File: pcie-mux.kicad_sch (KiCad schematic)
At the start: 25 parts, among them Q4 BSS138PW,115, Q5 BSS138PW,115, SW1 SW_CVS-02B, U11 SY75602BTWL-TR, U4 TMUXHS4412RUAR, U8 74LVC1G157-Q100H_SOT457

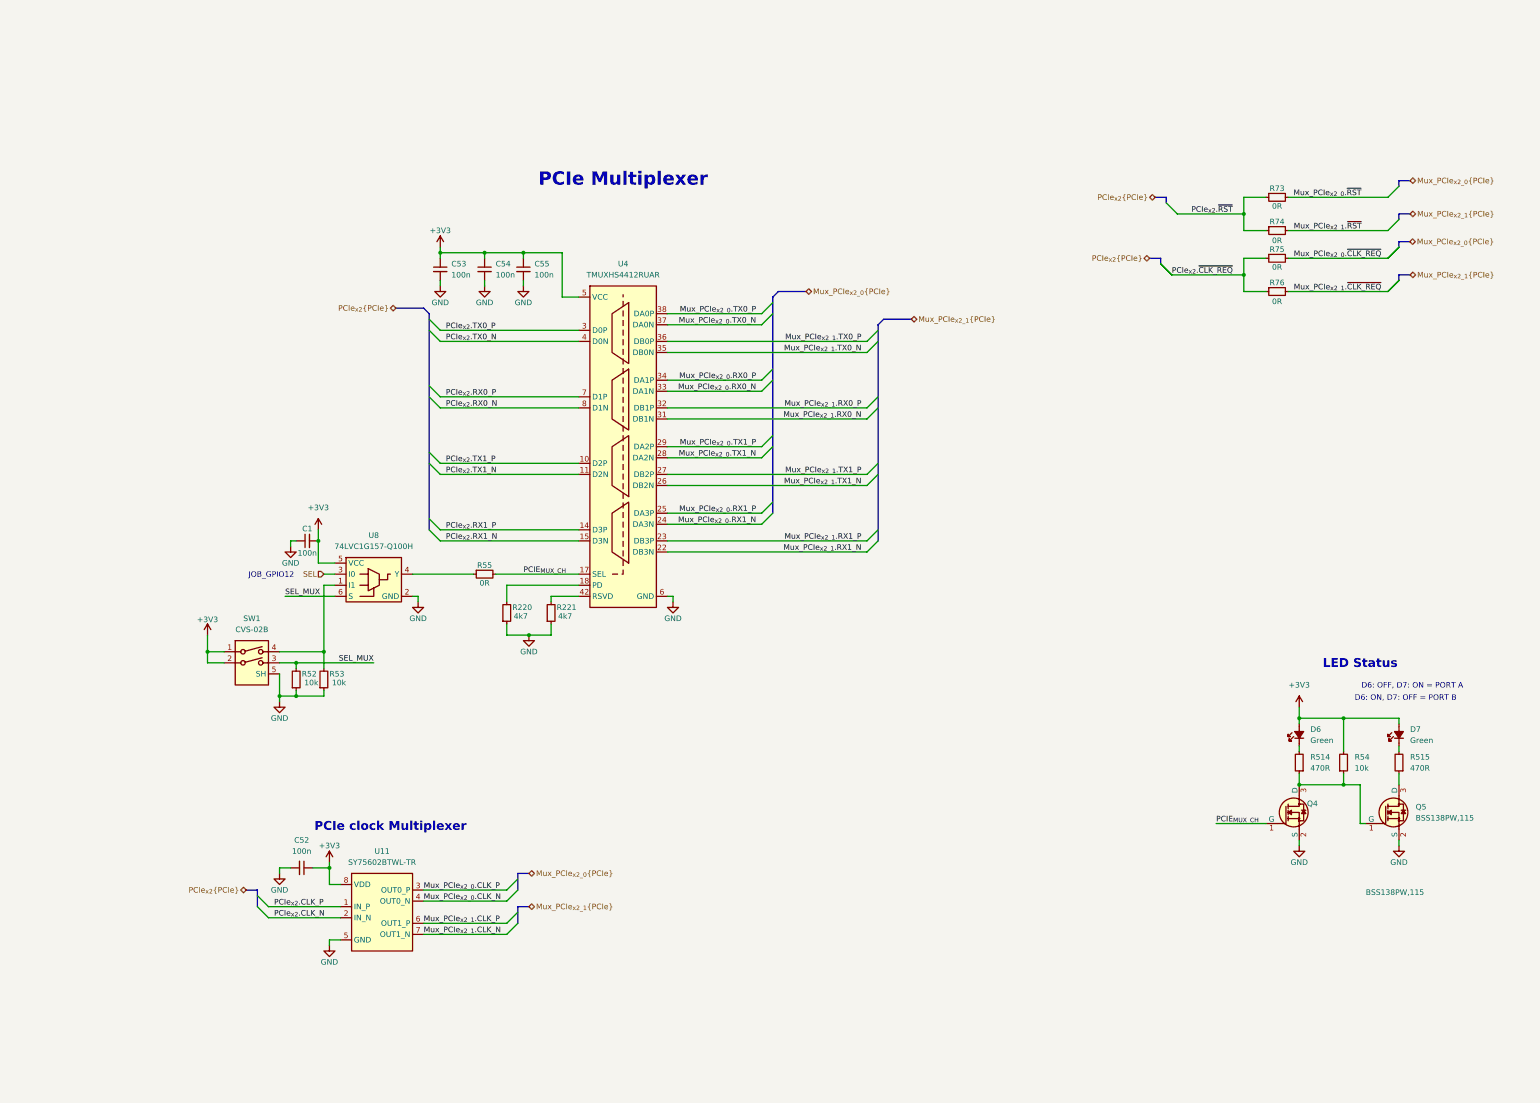
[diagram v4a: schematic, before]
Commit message: [#100765] WIP: Apply review changes
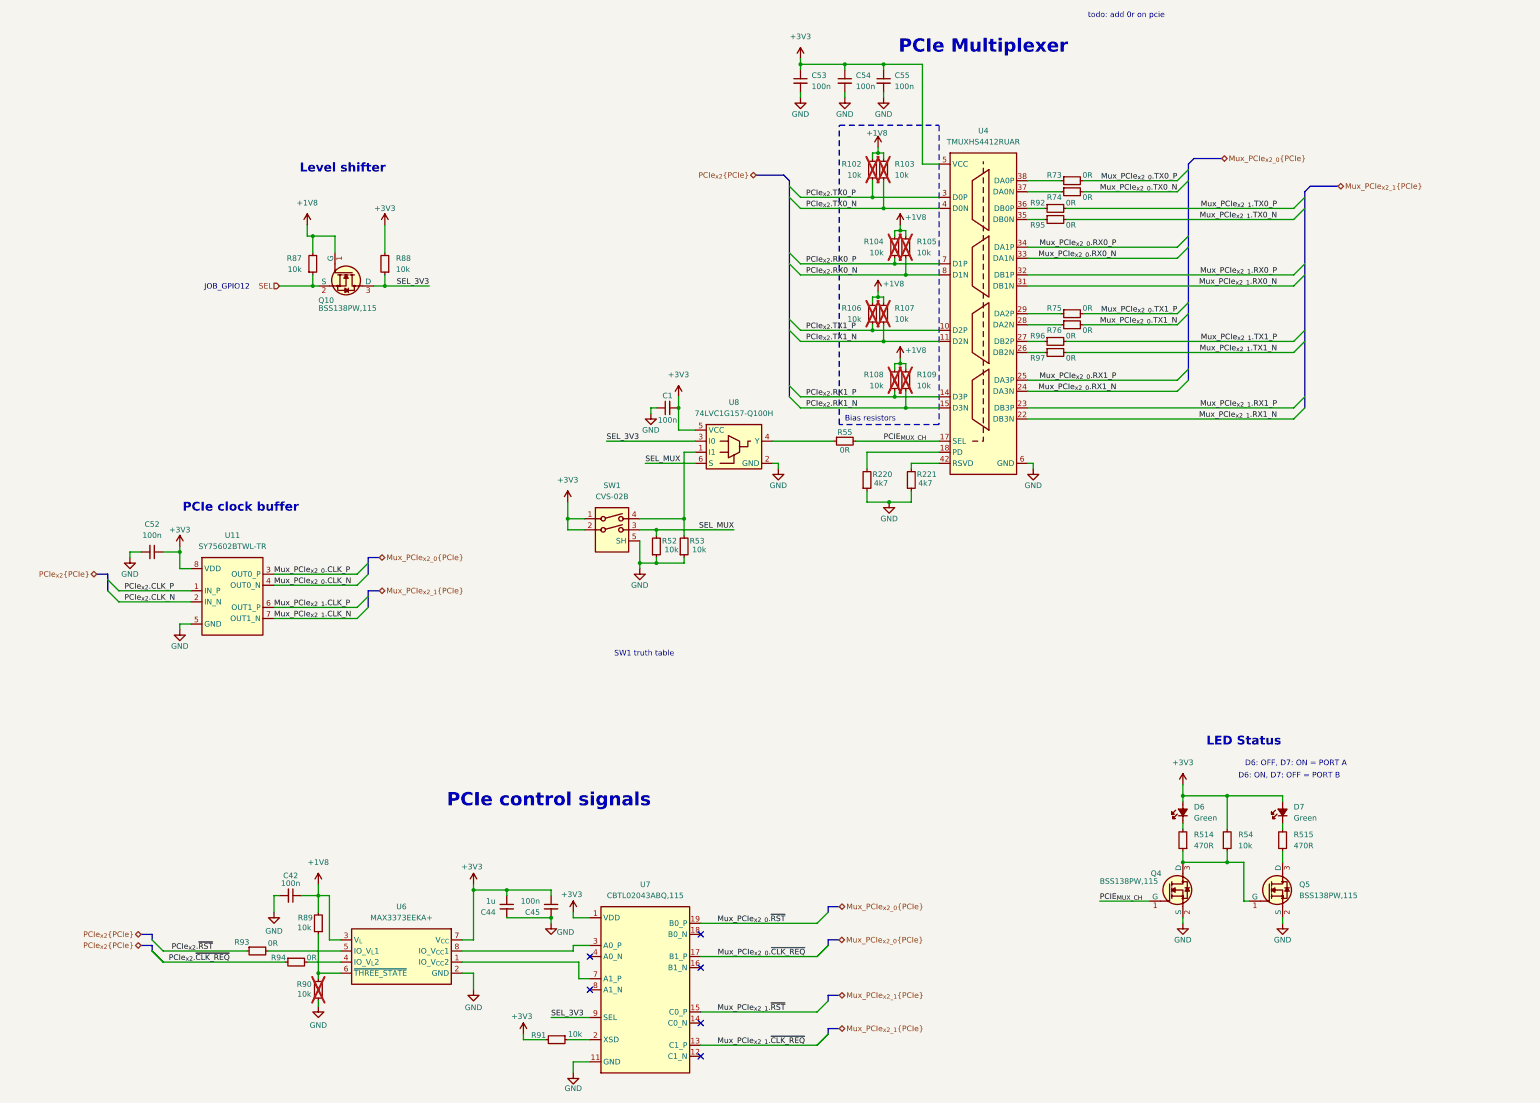
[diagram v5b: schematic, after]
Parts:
- added C42, C45: C_100n_0402, antmicro-footprints:C_0402_1005Metric, symbol antmicroCapacitors0402:C_100n_0402
- added C44: C_1u_0402, antmicro-footprints:C_0402_1005Metric, symbol antmicroCapacitors0402:C_1u_0402
- added Q10: BSS138PW,115, antmicro-footprints:SC70-3, symbol antmicroTransistorsFETsMOSFETsSingle:BSS138PW,115
- added R102, R103, R104, R105, R106, R107, R108, R109, R87, R88, R89, R90, R91: R_10k_0402, antmicro-footprints:R_0402_1005Metric, symbol antmicroResistors0402:R_10k_0402
- added R92, R93, R94, R95, R96, R97: R_0R_0402, antmicro-footprints:R_0402_1005Metric, symbol antmicroResistors0402:R_0R_0402
- added U6: MAX3373EEKA+, antmicro-footprints:SOT-23-8, symbol antmicroLogicTranslatorsLevelShifters:MAX3373EEKA+
- added U7: CBTL02043ABQ, antmicro-footprints:DHVQFN-20-1EP_2.5x4.5_P0.5mm, symbol antmicroLogicSignalSwitchesMultiplexersDecoders:CBTL02043ABQ
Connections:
- net +3V3: now also C44.1, C45.1, R88.2, R91.2, U6.7 (V_{CC}), U7.1 (VDD), U7.10 (VDD), U7.6 (VDD)
- net GND: now also C42.2, C44.2, C45.2, R90.1, U6.2 (GND), U7.11 (GND), U7.20 (GND), U7.21 (GND), U7.5 (GND)
- net Mux_PCIe_{x2_0}.TX0_N: now also R74.2; no longer U4.37 (DA0N)
- net Mux_PCIe_{x2_0}.TX0_P: now also R73.2; no longer U4.38 (DA0P)
- net Mux_PCIe_{x2_0}.TX1_N: now also R76.2; no longer U4.28 (DA2N)
- net Mux_PCIe_{x2_0}.TX1_P: now also R75.2; no longer U4.29 (DA2P)
- net Mux_PCIe_{x2_0}.~{CLK_REQ}: now also U7.17 (B1_P); no longer R75.2
- net Mux_PCIe_{x2_0}.~{RST}: now also U7.19 (B0_P); no longer R73.2
- net Mux_PCIe_{x2_1}.TX0_N: now also R95.2; no longer U4.35 (DB0N)
- net Mux_PCIe_{x2_1}.TX0_P: now also R92.2; no longer U4.36 (DB0P)
- net Mux_PCIe_{x2_1}.TX1_N: now also R97.2; no longer U4.26 (DB2N)
- net Mux_PCIe_{x2_1}.TX1_P: now also R96.2; no longer U4.27 (DB2P)
- net Mux_PCIe_{x2_1}.~{CLK_REQ}: now also U7.13 (C1_P); no longer R76.2
- net Mux_PCIe_{x2_1}.~{RST}: now also U7.15 (C0_P); no longer R74.2
- net PCIe_{x2}.RX0_N: now also R105.1
- net PCIe_{x2}.RX0_P: now also R104.1
- net PCIe_{x2}.RX1_N: now also R109.1
- net PCIe_{x2}.RX1_P: now also R108.1
- net PCIe_{x2}.TX0_N: now also R103.1
- net PCIe_{x2}.TX0_P: now also R102.1
- net PCIe_{x2}.TX1_N: now also R107.1
- net PCIe_{x2}.TX1_P: now also R106.1
- net PCIe_{x2}.~{CLK_REQ}: now also R94.1; no longer R75.1, R76.1
- net PCIe_{x2}.~{RST}: now also R93.1; no longer R73.1, R74.1
- net SEL: now also Q10.2 (S), R87.1; no longer U8.3 (I0)
- new net: R75.1, U4.29 (DA2P)
- new net: R92.1, U4.36 (DB0P)
- new net: R73.1, U4.38 (DA0P)
- new net: R91.1, U7.2 (XSD)
- new net: U6.8 (IO_V_{CC}1), U7.3 (A0_P)
- new net: U6.1 (IO_V_{CC}2), U7.7 (A1_P)
- new net: R89.1, R90.2, U6.6 (~{THREE_STATE})
- new net: R74.1, U4.37 (DA0N)
- new net: R95.1, U4.35 (DB0N)
- new net: R97.1, U4.26 (DB2N)
- new net: R93.2, U6.5 (IO_V_{L}1)
- new net: R96.1, U4.27 (DB2P)
- new net: R76.1, U4.28 (DA2N)
- new net: R94.2, U6.4 (IO_V_{L}2)
- new net +1V8: C42.1, Q10.1 (G), R102.2, R103.2, R104.2, R105.2, R106.2, R107.2, R108.2, R109.2, R87.2, R89.2, U6.3 (V_{L})
- new net SEL_3V3: Q10.3 (D), R88.1, U7.9 (SEL), U8.3 (I0)
- no-connect marks 0 -> 6
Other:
- note added: "Bias resistors"
- note added: "Level shifter"
- note added: "PCIe clock buffer"
- note added: "PCIe control signals"
- note added: "SW1 truth table"
- note added: "todo: add 0r on pcie"
- note removed: "PCIe clock Multiplexer"
- moved on the sheet: C1, C52, C53, C54, C55, D6, D7, Q4, Q5, R220, R221, R514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

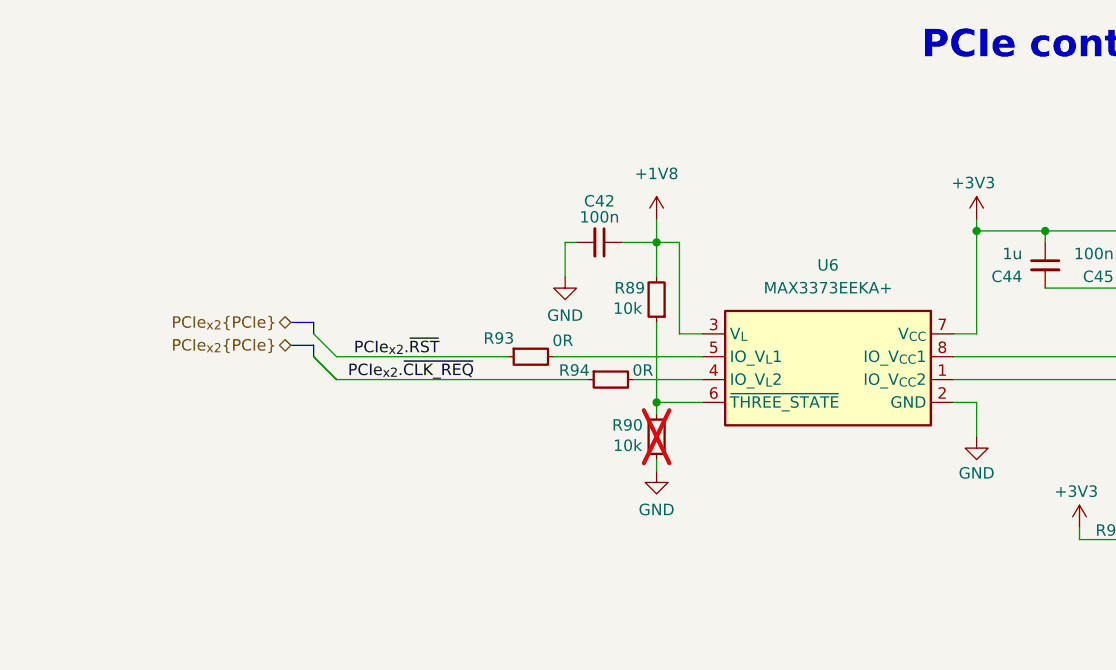
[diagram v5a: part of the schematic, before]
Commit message: [#100765] Change MAX3373EEKA+ to NTS0302JKZ
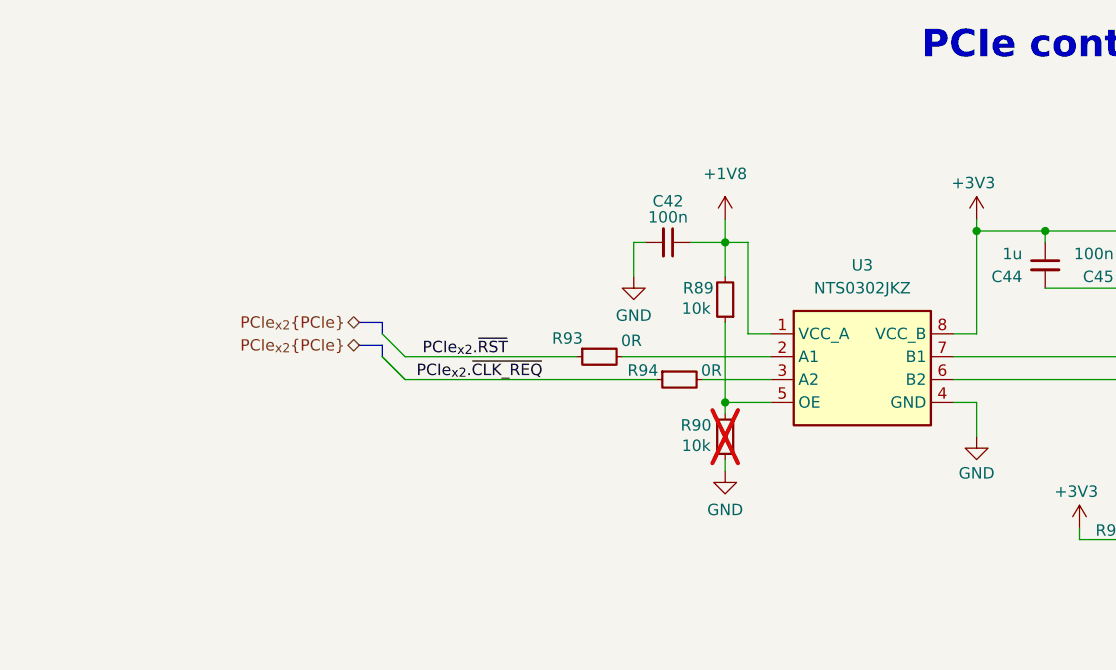
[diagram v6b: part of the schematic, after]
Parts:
- removed U6: MAX3373EEKA+, antmicro-footprints:SOT-23-8, symbol antmicroLogicTranslatorsLevelShifters:MAX3373EEKA+
- added U3: NTS0302JKZ, antmicro-footprints:X2SON8_1.4x1x0.32mm_P0.35mm, symbol antmicroLogicTranslatorsLevelShifters:NTS0302JKZ
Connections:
- net +1V8: now also U3.1 (VCC_A)
- net +3V3: now also U3.8 (VCC_B)
- net GND: now also U3.4 (GND)
- net at U7.3 (A0_P): now also U3.7 (B1)
- net at U7.7 (A1_P): now also U3.6 (B2)
- net at R89.1, R90.2: now also U3.5 (OE)
- net at R93.2: now also U3.2 (A1)
- net at R94.2: now also U3.3 (A2)
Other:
- moved on the sheet: C42, R89, R90, R93, R94

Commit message: [#100765] Apply fixes from review
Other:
- note added: "Status LEDs"
- note removed: "LED Status"
- note removed: "todo: add 0r on pcie"
- moved on the sheet: C1, C42, C44, C45, C52, C53, C54, C55, D6, D7, Q10, Q4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

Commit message: [#100765] Reset designators
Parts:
- renumbered C52 to C60, C1 to C61, C42 to C62, C53 to C63, C54 to C64, C55 to C65, C44 to C66, C45 to C67, D6 to D8, D7 to D9, Q4 to Q6, Q10 to Q7, Q5 to Q8, R107 to R100, R104 to R101, R108 to R102, R105 to R103, R109 to R104, R221 to R105, R91 to R106, R92 to R107, R95 to R108, R96 to R109, R97 to R110, R73 to R111, R74 to R112, R75 to R113, R76 to R114, R514 to R84, R87 to R85, R54 to R86, R88 to R87, R515 to R88, R93 to R89, R94 to R90, R52 to R91, R53 to R92, R89 to R93, R90 to R94, R55 to R95, R220 to R96, R102 to R97, R106 to R98, R103 to R99, U4 to U10, U7 to U11, U11 to U7, U3 to U9
